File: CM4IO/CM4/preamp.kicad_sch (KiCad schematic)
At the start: 23 parts, among them IC1 OPA659IDBVR, IC2 OPA659IDBVR, IC3 LMH6643MAX_NOPB, J1 SMA Edge

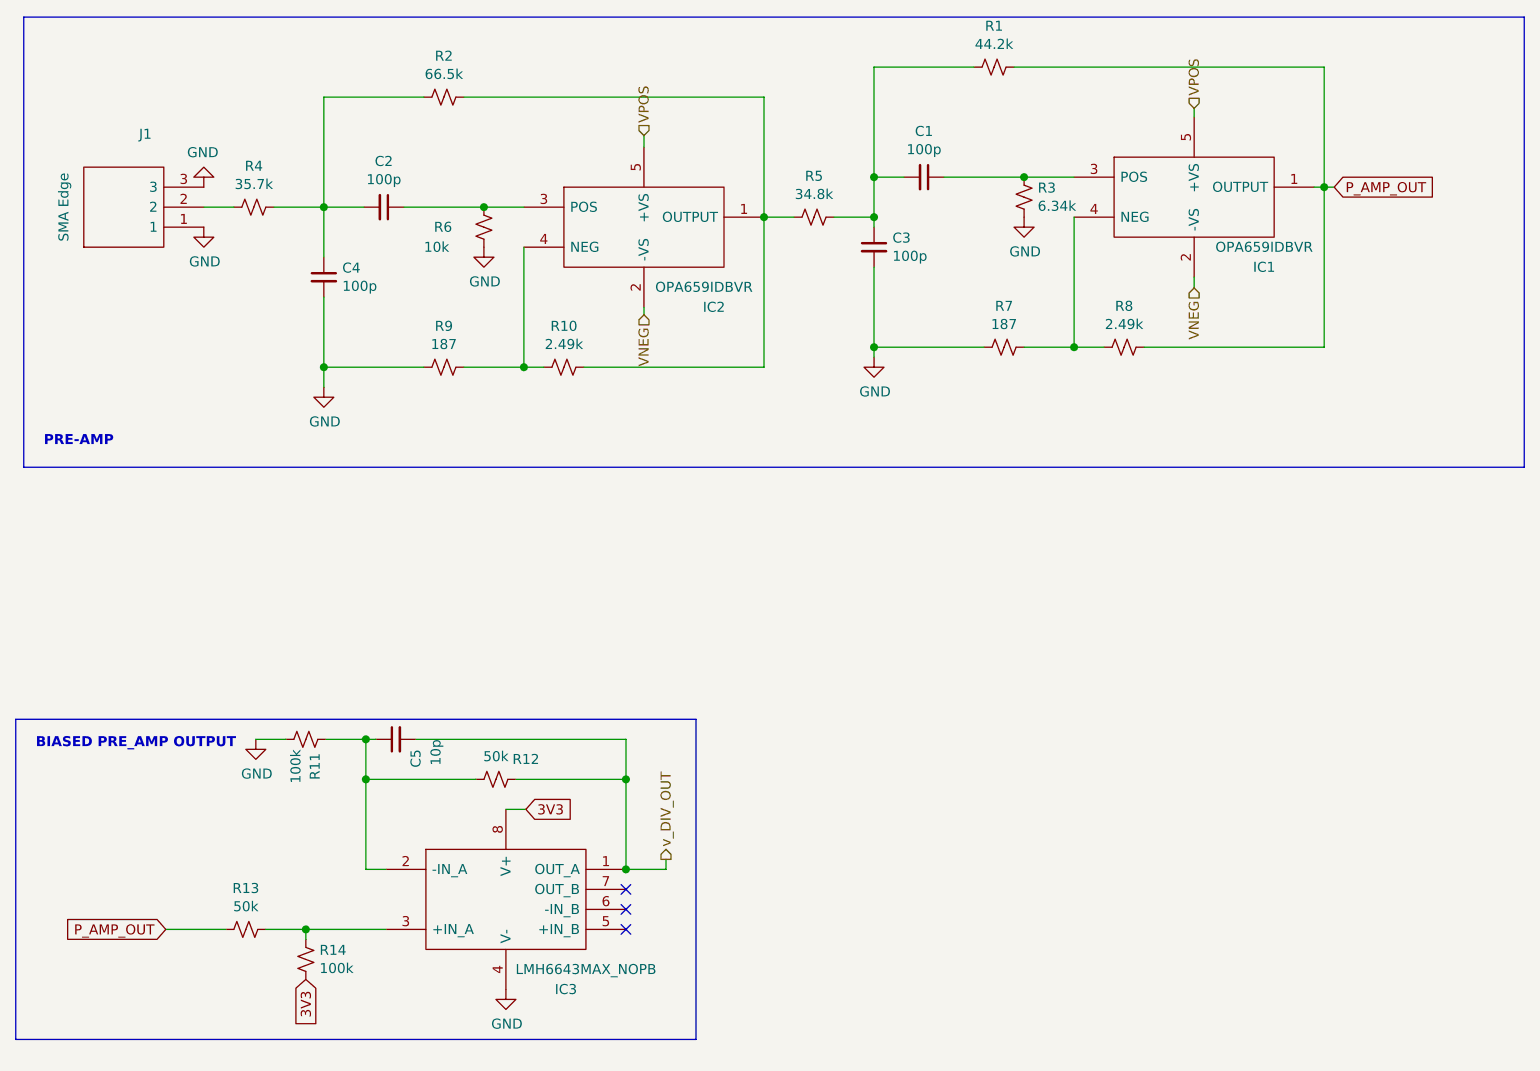
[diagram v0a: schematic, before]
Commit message: Initial CM4IO board design
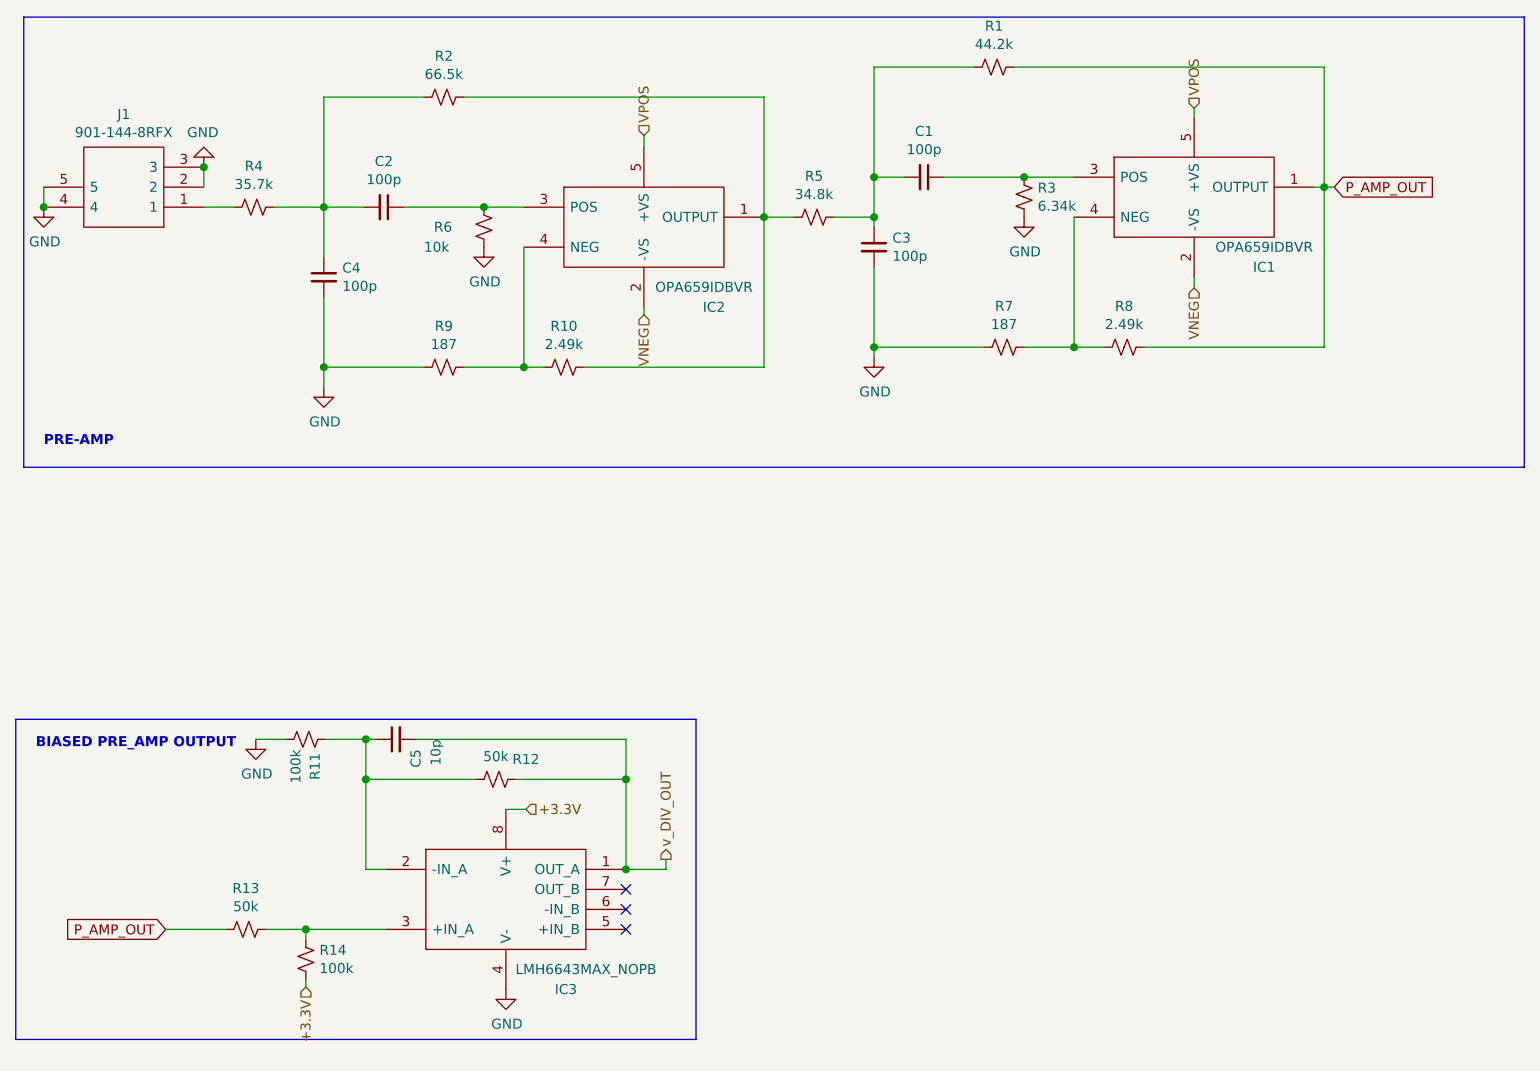
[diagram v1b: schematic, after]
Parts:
- removed J1: SMA Edge, SamacSys_Parts:142-0701-851, symbol SamacSys_Parts:142-0701-851
- added J1: 901-144-8RFX, 9011448RFX, symbol SamacSys_Parts:901-144-8RFX
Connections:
- net GND: now also J1.2, J1.3, J1.4, J1.5
- net at R4.2: now also J1.1
- net 3V3 renamed +3.3V
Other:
- title: (none) -> 90 - 150KHz 40dB band pass pre-amp
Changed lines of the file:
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@@
   (page 3 6)
   (paper "A4")
+  (title_block
+    (title "90 - 150KHz 40dB band pass pre-amp")
+  )
+  (junction (at 43.434 61.1124) (diameter 1.016) (color 0 0 0 0))
+  (junction (at 63.754 56.0324) (diameter 1.016) (color 0 0 0 0))
   (junction (at 76.708 152.8064) (diameter 1.016) (color 0 0 0 0))
   (junction (at 78.994 61.1124) (diameter 1.016) (color 0 0 0 0))
@@
   (junction (at 205.994 58.5724) (diameter 1.016) (color 0 0 0 0))
   (no_connect (at 117.348 147.7264))
+  (no_connect (at 117.348 150.2664))
   (no_connect (at 117.348 152.8064))
-  (no_connect (at 117.348 150.2664))
+  (wire (pts (xy 43.434 58.5724) (xy 43.434 61.1124))
+    (stroke (width 0) (type solid) (color 0 0 0 0))
+  )
+  (wire (pts (xy 63.754 56.0324) (xy 63.754 58.5724))
+    (stroke (width 0) (type solid) (color 0 0 0 0))
+  )
   (wire (pts (xy 63.754 61.1124) (xy 67.564 61.1124))
     (stroke (width 0) (type solid) (color 0 0 0 0))
@@
   )
   (wire (pts (xy 76.708 152.8064) (xy 76.708 154.0764))
+    (stroke (width 0) (type solid) (color 0 0 0 0))
+  )
+  (wire (pts (xy 76.708 159.1564) (xy 76.708 160.1216))
     (stroke (width 0) (type solid) (color 0 0 0 0))
   )
@@
     (effects (font (size 1.27 1.27)) (justify right))
   )
-  (global_label "3V3" (shape input) (at 76.708 159.1564 270)
-    (effects (font (size 1.27 1.27)) (justify right))
-  )
-  (global_label "3V3" (shape input) (at 104.648 137.5664 0)
-    (effects (font (size 1.27 1.27)) (justify left))
-  )
   (global_label "P_AMP_OUT" (shape input) (at 207.264 58.5724 0)
     (effects (font (size 1.27 1.27)) (justify left))
   )
+  (hierarchical_label "+3.3V" (shape input) (at 76.708 160.1216 270)
+    (effects (font (size 1.27 1.27)) (justify right))
+  )
+  (hierarchical_label "+3.3V" (shape input) (at 104.648 137.5664 0)
+    (effects (font (size 1.27 1.27)) (justify left))
+  )
   (hierarchical_label "VPOS" (shape input) (at 119.634 52.0192 90)
     (effects (font (size 1.27 1.27)) (justify left))
@@
     (effects (font (size 1.27 1.27)) (justify right))
   )
-  (symbol (lib_id "power:GND") (at 63.754 58.5724 180) (unit 1)
-    (in_bom yes) (on_board yes)
-    (property "Reference" "#PWR0106" (id 0) (at 63.754 52.2224 0)
-      (effects (font (size 1.27 1.27)) hide)
-    )
-    (property "Value" "GND" (id 1) (at 63.627 54.1782 0))
-    (property "Footprint" "" (id 2) (at 63.754 58.5724 0)
-      (effects (font (size 1.27 1.27)) hide)
-    )
-    (property "Datasheet" "" (id 3) (at 63.754 58.5724 0)
-      (effects (font (size 1.27 1.27)) hide)
-    )
-  )
-  (symbol (lib_id "power:GND") (at 63.754 63.6524 0) (unit 1)
-    (in_bom yes) (on_board yes)
-    (property "Reference" "#PWR0105" (id 0) (at 63.754 70.0024 0)
-      (effects (font (size 1.27 1.27)) hide)
-    )
-    (property "Value" "GND" (id 1) (at 63.881 68.0466 0))
-    (property "Footprint" "" (id 2) (at 63.754 63.6524 0)
-      (effects (font (size 1.27 1.27)) hide)
-    )
-    (property "Datasheet" "" (id 3) (at 63.754 63.6524 0)
+  (symbol (lib_id "power:GND") (at 43.434 61.1124 0) (unit 1)
+    (in_bom yes) (on_board yes)
+    (property "Reference" "#PWR0105" (id 0) (at 43.434 67.4624 0)
+      (effects (font (size 1.27 1.27)) hide)
+    )
+    (property "Value" "GND" (id 1) (at 43.561 65.5066 0))
+    (property "Footprint" "" (id 2) (at 43.434 61.1124 0)
+      (effects (font (size 1.27 1.27)) hide)
+    )
+    (property "Datasheet" "" (id 3) (at 43.434 61.1124 0)
+      (effects (font (size 1.27 1.27)) hide)
+    )
+  )
+  (symbol (lib_id "power:GND") (at 63.754 56.0324 180) (unit 1)
+    (in_bom yes) (on_board yes)
+    (property "Reference" "#PWR0106" (id 0) (at 63.754 49.6824 0)
+      (effects (font (size 1.27 1.27)) hide)
+    )
+    (property "Value" "GND" (id 1) (at 63.627 51.6382 0))
+    (property "Footprint" "" (id 2) (at 63.754 56.0324 0)
+      (effects (font (size 1.27 1.27)) hide)
+    )
+    (property "Datasheet" "" (id 3) (at 63.754 56.0324 0)
       (effects (font (size 1.27 1.27)) hide)
     )
@@
     )
   )
-  (symbol (lib_id "SamacSys_Parts:142-0701-851") (at 63.754 63.6524 90) (unit 1)
-    (in_bom yes) (on_board yes)
-    (property "Reference" "J1" (id 0) (at 56.3372 51.8414 90))
-    (property "Value" "SMA Edge" (id 1) (at 45.974 61.1124 0))
-    (property "Footprint" "SamacSys_Parts:142-0701-851" (id 2) (at 48.514 54.7624 0)
-      (effects (font (size 1.27 1.27)) (justify left) hide)
-    )
-    (property "Datasheet" "http://www.belfuse.com/resources/Johnson/drawings/dr-1420701851.pdf" (id 3) (at 51.054 54.7624 0)
-      (effects (font (size 1.27 1.27)) (justify left) hide)
-    )
-    (property "Description" "SMA 50 Ohm End Launch Jack Receptacle - Tab Contact" (id 4) (at 53.594 54.7624 0)
-      (effects (font (size 1.27 1.27)) (justify left) hide)
-    )
-    (property "Manufacturer_Name" "Cinch" (id 5) (at 58.674 54.7624 0)
-      (effects (font (size 1.27 1.27)) (justify left) hide)
-    )
-    (property "Manufacturer_Part_Number" "142-0701-851" (id 6) (at 61.214 54.7624 0)
-      (effects (font (size 1.27 1.27)) (justify left) hide)
-    )
-    (property "Mouser Part Number" "530-142-0701-851" (id 7) (at 63.754 54.7624 0)
-      (effects (font (size 1.27 1.27)) (justify left) hide)
-    )
-    (property "Mouser Price/Stock" "https://www.mouser.com/Search/Refine.aspx?Keyword=530-142-0701-851" (id 8) (at 66.294 54.7624 0)
-      (effects (font (size 1.27 1.27)) (justify left) hide)
-    )
-    (property "RS Part Number" "8857532" (id 9) (at 68.834 54.7624 0)
-      (effects (font (size 1.27 1.27)) (justify left) hide)
-    )
-    (property "RS Price/Stock" "http://uk.rs-online.com/web/p/products/8857532" (id 10) (at 71.374 54.7624 0)
-      (effects (font (size 1.27 1.27)) (justify left) hide)
-    )
-    (property "Allied_Number" "70090523" (id 11) (at 73.914 54.7624 0)
-      (effects (font (size 1.27 1.27)) (justify left) hide)
-    )
-    (property "Allied Price/Stock" "https://www.alliedelec.com/johnson-cinch-connectivity-solutions-142-0701-851/70090523/" (id 12) (at 76.454 54.7624 0)
-      (effects (font (size 1.27 1.27)) (justify left) hide)
-    )
+  (symbol (lib_id "SamacSys_Parts:901-144-8RFX") (at 63.754 61.1124 180) (unit 1)
+    (in_bom yes) (on_board yes)
+    (property "Reference" "J1" (id 0) (at 53.594 49.333 0))
+    (property "Value" "901-144-8RFX" (id 1) (at 53.594 51.6317 0))
+    (property "Footprint" "9011448RFX" (id 2) (at 47.244 63.6524 0)
+      (effects (font (size 1.27 1.27)) (justify left) hide)
+    )
+    (property "Datasheet" "https://componentsearchengine.com/Datasheets/1/901-144-8RFX.pdf" (id 3) (at 47.244 61.1124 0)
+      (effects (font (size 1.27 1.27)) (justify left) hide)
+    )
+    (property "Description" "AMPHENOL RF - 901-144-8RFX - RF / Coaxial Connector, SMA Coaxial, Straight Jack, Solder, 50 ohm, Beryllium Copper" (id 4) (at 47.244 58.5724 0)
+      (effects (font (size 1.27 1.27)) (justify left) hide)
+    )
+    (property "Height" "9.53" (id 5) (at 47.244 56.0324 0)
+      (effects (font (size 1.27 1.27)) (justify left) hide)
+    )
+    (property "Manufacturer_Name" "Amphenol" (id 6) (at 47.244 53.4924 0)
+      (effects (font (size 1.27 1.27)) (justify left) hide)
+    )
+    (property "Manufacturer_Part_Number" "901-144-8RFX" (id 7) (at 47.244 50.9524 0)
+      (effects (font (size 1.27 1.27)) (justify left) hide)
+    )
+    (property "Arrow Part Number" "901-144-8RFX" (id 8) (at 47.244 48.4124 0)
+      (effects (font (size 1.27 1.27)) (justify left) hide)
+    )
+    (property "Arrow Price/Stock" "https://www.arrow.com/en/products/901-144-8rfx/amphenol-rf" (id 9) (at 47.244 45.8724 0)
+      (effects (font (size 1.27 1.27)) (justify left) hide)
+    )
+    (property "Mouser Part Number" "523-901-144-8RFX" (id 10) (at 47.244 43.3324 0)
+      (effects (font (size 1.27 1.27)) (justify left) hide)
+    )
+    (property "Mouser Price/Stock" "https://www.mouser.co.uk/ProductDetail/Amphenol-RF/901-144-8RFX?qs=jpOL8GWAqat%252BbPjbt8toTg%3D%3D" (id 11) (at 47.244 40.7924 0)
+      (effects (font (size 1.27 1.27)) (justify left) hide)
+    )
